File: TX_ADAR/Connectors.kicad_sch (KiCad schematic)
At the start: 10 parts, among them J1 Conn_Coaxial, J11 RJ45_LED_Shielded, J12 RJ45_LED_Shielded, J13 Conn_Coaxial, J14 Conn_Coaxial, J15 FX8-120S-SV21, J16 RJ45_LED_Shielded, J17 Conn_Coaxial, J18 Conn_Coaxial, J2 Conn_Coaxial

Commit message: Got footprints to work
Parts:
- J15: footprint FX8_120S_SV_21_:HRS_FX8-120S-SV_21_ -> footprints:CONN120_FX8-120S-SV_HIR
- J2: footprint (none) -> 142_1701_831:BEL_142-1701-831
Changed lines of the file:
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@@
 			)
 		)
-		(property "Footprint" "FX8_120S_SV_21_:HRS_FX8-120S-SV_21_"
+		(property "Footprint" "footprints:CONN120_FX8-120S-SV_HIR"
 			(at 146.05 20.32 0)
 			(hide yes)
@@
 			)
 		)
-		(property "Footprint" "FX8_120S_SV_21_:HRS_FX8-120S-SV_21_"
+		(property "Footprint" "footprints:CONN120_FX8-120S-SV_HIR"
 			(at 241.3 20.32 0)
 			(hide yes)
@@
 			)
 		)
-		(property "Footprint" ""
+		(property "Footprint" "142_1701_831:BEL_142-1701-831"
 			(at 57.15 19.05 0)
 			(hide yes)
@@
 			)
 		)
-		(property "Footprint" "FX8_120S_SV_21_:HRS_FX8-120S-SV_21_"
+		(property "Footprint" "footprints:CONN120_FX8-120S-SV_HIR"
 			(at 195.58 20.32 0)
 			(hide yes)

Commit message: Setting up layout plan
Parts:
- J15: footprint footprints:CONN120_FX8-120S-SV_HIR -> 120Conn footprints:CONN120_FX8-120S-SV_HIR
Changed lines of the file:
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@@
 			)
 		)
-		(property "Footprint" "footprints:CONN120_FX8-120S-SV_HIR"
+		(property "Footprint" "120Conn footprints:CONN120_FX8-120S-SV_HIR"
 			(at 146.05 20.32 0)
 			(hide yes)
@@
 			)
 		)
-		(property "Footprint" "footprints:CONN120_FX8-120S-SV_HIR"
+		(property "Footprint" "120Conn footprints:CONN120_FX8-120S-SV_HIR"
 			(at 241.3 20.32 0)
 			(hide yes)
@@
 			)
 		)
-		(property "Footprint" "footprints:CONN120_FX8-120S-SV_HIR"
+		(property "Footprint" "120Conn footprints:CONN120_FX8-120S-SV_HIR"
 			(at 195.58 20.32 0)
 			(hide yes)

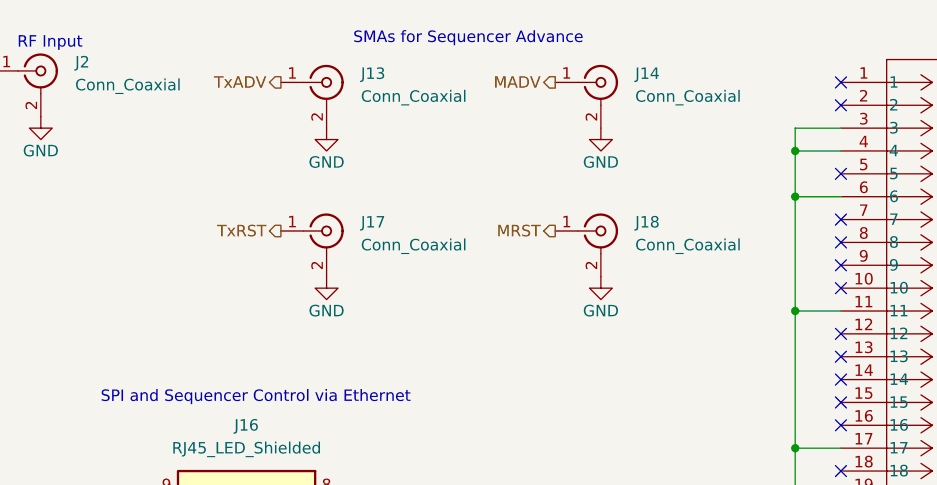
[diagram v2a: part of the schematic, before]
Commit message: Finished up adding footprints. Removed unnecessary switches for the TxRST and MRST
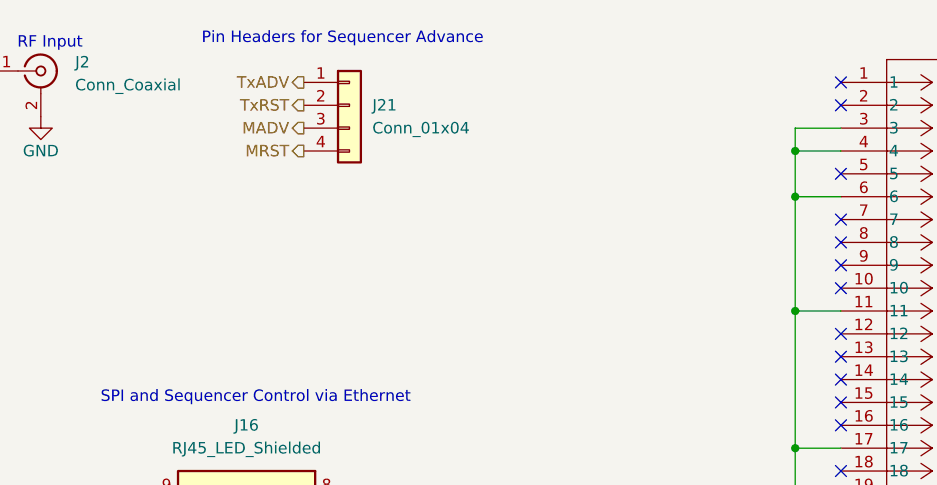
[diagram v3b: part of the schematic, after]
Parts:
- removed J13, J14, J17, J18: Conn_Coaxial, Connector_Coaxial:SMA_Amphenol_132134-10_Vertical, symbol Connector:Conn_Coaxial
- added J21: Conn_01x04, Connector_PinHeader_2.54mm:PinHeader_1x04_P2.54mm_Vertical, symbol Connector_Generic:Conn_01x04
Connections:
- net MADV: now also J21.3 (Pin_3)
- net MRST: now also J21.4 (Pin_4)
- net TxADV: now also J21.1 (Pin_1)
- net TxRST: now also J21.2 (Pin_2)
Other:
- note added: "Pin Headers for Sequencer Advance"
- note removed: "SMAs for Sequencer Advance"

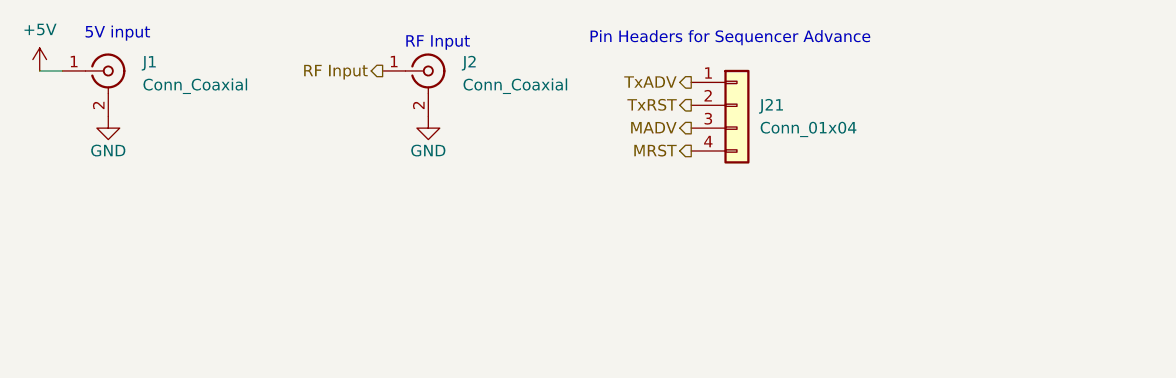
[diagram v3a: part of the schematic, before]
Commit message: Fixed footprint and meddled with the layout
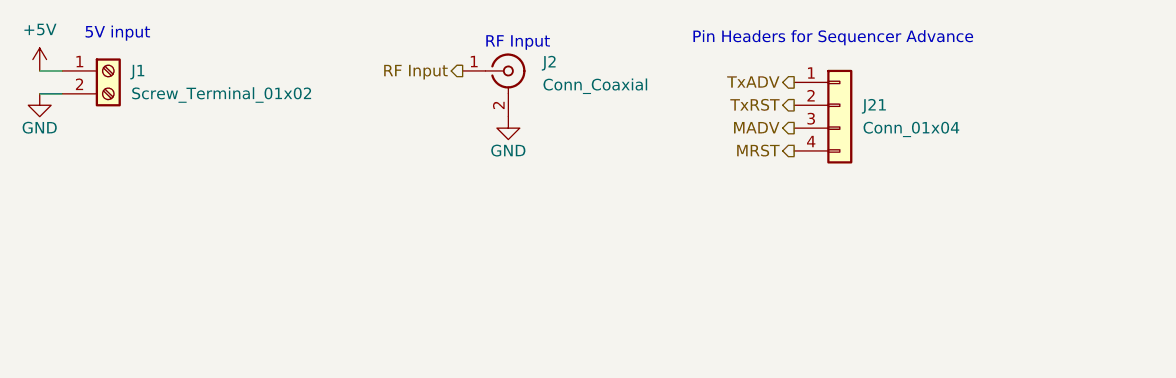
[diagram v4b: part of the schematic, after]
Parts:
- removed J1: Conn_Coaxial, Connector_Coaxial:SMA_Amphenol_132289_EdgeMount, symbol Connector:Conn_Coaxial
- added J1: Screw_Terminal_01x02, TerminalBlock_Phoenix:TerminalBlock_Phoenix_MKDS-1,5-2-5.08_1x02_P5.08mm_Horizontal, symbol Connector:Screw_Terminal_01x02
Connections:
- net +5V: now also J1.1 (Pin_1)
- net GND: now also J1.2 (Pin_2)
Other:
- moved on the sheet: J2, J21
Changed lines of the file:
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@@
 	(text "RF Input"
 		(exclude_from_sim no)
-		(at 58.166 16.002 0)
+		(at 67.056 16.002 0)
 		(effects
 			(font
@@
 	(text "Pin Headers for Sequencer Advance"
 		(exclude_from_sim no)
-		(at 90.678 15.494 0)
+		(at 102.108 15.494 0)
 		(effects
 			(font
@@
 	(wire
 		(pts
+			(xy 13.97 21.59) (xy 16.51 21.59)
+		)
+		(stroke
+			(width 0)
+			(type default)
+		)
+	)
+	(wire
+		(pts
 			(xy 236.22 116.84) (xy 241.3 116.84)
 		)
@@
 	(hierarchical_label "TxRST"
 		(shape output)
-		(at 86.36 22.86 180)
+		(at 97.79 22.86 180)
 		(effects
 			(font
@@
 	(hierarchical_label "MADV"
 		(shape output)
-		(at 86.36 25.4 180)
+		(at 97.79 25.4 180)
 		(effects
 			(font
@@
 	(hierarchical_label "RF Input"
 		(shape output)
-		(at 52.07 19.05 180)
+		(at 60.96 19.05 180)
 		(effects
 			(font
@@
 	(hierarchical_label "MRST"
 		(shape output)
-		(at 86.36 27.94 180)
+		(at 97.79 27.94 180)
 		(effects
 			(font
@@
 	(hierarchical_label "TxADV"
 		(shape output)
-		(at 86.36 20.32 180)
+		(at 97.79 20.32 180)
 		(effects
 			(font
@@
 	)
 	(symbol
+		(lib_id "Connector:Screw_Terminal_01x02")
+		(at 21.59 19.05 0)
+		(unit 1)
+		(body_style 1)
+		(exclude_from_sim no)
+		(in_bom yes)
+		(on_board yes)
+		(in_pos_files yes)
+		(dnp no)
+		(fields_autoplaced yes)
+		(property "Reference" "J1"
+			(at 24.13 19.0499 0)
+			(show_name no)
+			(do_not_autoplace no)
+			(effects
+				(font
+					(size 1.27 1.27)
+				)
+				(justify left)
+			)
+		)
+		(property "Value" "Screw_Terminal_01x02"
+			(at 24.13 21.5899 0)
+			(show_name no)
+			(do_not_autoplace no)
+			(effects
+				(font
+					(size 1.27 1.27)
+				)
+				(justify left)
+			)
+		)
+		(property "Footprint" "TerminalBlock_Phoenix:TerminalBlock_Phoenix_MKDS-1,5-2-5.08_1x02_P5.08mm_Horizontal"
+			(at 21.59 19.05 0)
+			(hide yes)
+			(show_name no)
+			(do_not_autoplace no)
+			(effects
+				(font
+					(size 1.27 1.27)
+				)
+			)
+		)
+		(property "Datasheet" ""
+			(at 21.59 19.05 0)
+			(hide yes)
+			(show_name no)
+			(do_not_autoplace no)
+			(effects
+				(font
+					(size 1.27 1.27)
+				)
+			)
+		)
+		(property "Description" "Generic screw terminal, single row, 01x02, script generated (kicad-library-utils/schlib/autogen/connector/)"
+			(at 21.59 19.05 0)
+			(hide yes)
+			(show_name no)
+			(do_not_autoplace no)
+			(effects
+				(font
+					(size 1.27 1.27)
+				)
+			)
+		)
+		(pin "1"
+		)
+		(pin "2"
+		)
+		(instances
+			(project "TX_ADAR"
+				(path "/5bb7bcfe-c6dc-48dd-b109-2cc47fd52212/5711866b-ad81-4828-9e56-17f3c1154618"
+					(reference "J1")
+					(unit 1)
+				)
+			)
+		)
+	)
+	(symbol
 		(lib_id "power:PWR_FLAG")
 		(at 40.64 66.04 0)
@@
 	(symbol
 		(lib_id "Connector_Generic:Conn_01x04")
-		(at 91.44 22.86 0)
+		(at 102.87 22.86 0)
 		(unit 1)
 		(body_style 1)
@@
 		(fields_autoplaced yes)
 		(property "Reference" "J21"
-			(at 93.98 22.86 0)
+			(at 105.41 22.86 0)
 			(show_name no)
 			(do_not_autoplace no)
@@
 		)
 		(property "Value" "Conn_01x04"
-			(at 93.98 25.4 0)
+			(at 105.41 25.4 0)
 			(show_name no)
 			(do_not_autoplace no)
@@
 		)
 		(property "Footprint" "Connector_PinHeader_2.54mm:PinHeader_1x04_P2.54mm_Vertical"
-			(at 91.44 22.86 0)
+			(at 102.87 22.86 0)
 			(hide yes)
 			(show_name no)
@@
 		)
 		(property "Datasheet" ""
-			(at 91.44 22.86 0)
+			(at 102.87 22.86 0)
 			(hide yes)
 			(show_name no)
@@
 		)
 		(property "Description" "Generic connector, single row, 01x04, script generated (kicad-library-utils/schlib/autogen/connector/)"
-			(at 91.44 22.86 0)
+			(at 102.87 22.86 0)
 			(hide yes)
 			(show_name no)
@@
 	(symbol
 		(lib_id "Connector:Conn_Coaxial")
-		(at 57.15 19.05 0)
+		(at 66.04 19.05 0)
 		(unit 1)
 		(body_style 1)
@@
 		(fields_autoplaced yes)
 		(property "Reference" "J2"
-			(at 60.96 18.0731 0)
+			(at 69.85 18.0731 0)
 			(show_name no)
 			(do_not_autoplace no)
@@
 		)
 		(property "Value" "Conn_Coaxial"
-			(at 60.96 20.6131 0)
+			(at 69.85 20.6131 0)
 			(show_name no)
 			(do_not_autoplace no)
@@
 		)
 		(property "Footprint" "142_1701_831:BEL_142-1701-831"
-			(at 57.15 19.05 0)
+			(at 66.04 19.05 0)
 			(hide yes)
 			(show_name no)
@@
 		)
 		(property "Datasheet" ""
-			(at 57.15 19.05 0)
+			(at 66.04 19.05 0)
 			(hide yes)
 			(show_name no)
@@
 		)
 		(property "Description" "coaxial connector (BNC, SMA, SMB, SMC, Cinch/RCA, LEMO, ...)"
-			(at 57.15 19.05 0)
+			(at 66.04 19.05 0)
 			(hide yes)
 			(show_name no)
@@
 	)
 	(symbol
-		(lib_id "Connector:Conn_Coaxial")
-		(at 21.59 19.05 0)
-		(unit 1)
-		(body_style 1)
-		(exclude_from_sim no)
-		(in_bom yes)
-		(on_board yes)
-		(in_pos_files yes)
-		(dnp no)
-		(fields_autoplaced yes)
-		(property "Reference" "J1"
-			(at 25.4 18.0731 0)
-			(show_name no)
-			(do_not_autoplace no)
-			(effects
-				(font
-					(size 1.27 1.27)
-				)
-				(justify left)
-			)
-		)
-		(property "Value" "Conn_Coaxial"
-			(at 25.4 20.6131 0)
-			(show_name no)
-			(do_not_autoplace no)
-			(effects
-				(font
-					(size 1.27 1.27)
-				)
-				(justify left)
-			)
-		)
-		(property "Footprint" "Connector_Coaxial:SMA_Amphenol_132289_EdgeMount"
-			(at 21.59 19.05 0)
-			(hide yes)
-			(show_name no)
-			(do_not_autoplace no)
-			(effects
-				(font
-					(size 1.27 1.27)
-				)
-			)
-		)
-		(property "Datasheet" ""
-			(at 21.59 19.05 0)
-			(hide yes)
-			(show_name no)
-			(do_not_autoplace no)
-			(effects
-				(font
-					(size 1.27 1.27)
-				)
-			)
-		)
-		(property "Description" "coaxial connector (BNC, SMA, SMB, SMC, Cinch/RCA, LEMO, ...)"
-			(at 21.59 19.05 0)
-			(hide yes)
-			(show_name no)
-			(do_not_autoplace no)
-			(effects
-				(font
-					(size 1.27 1.27)
-				)
-			)
-		)
-		(pin "1"
-		)
-		(pin "2"
-		)
-		(instances
-			(project "TX_ADAR"
-				(path "/5bb7bcfe-c6dc-48dd-b109-2cc47fd52212/5711866b-ad81-4828-9e56-17f3c1154618"
-					(reference "J1")
-					(unit 1)
-				)
-			)
-		)
-	)
-	(symbol
 		(lib_id "power:GND")
-		(at 57.15 24.13 0)
+		(at 66.04 24.13 0)
 		(unit 1)
 		(body_style 1)
@@
 		(dnp no)
 		(property "Reference" "#PWR010"
-			(at 57.15 30.48 0)
+			(at 66.04 30.48 0)
 			(hide yes)
 			(show_name no)
@@
 		)
 		(property "Value" "GND"
-			(at 57.15 27.94 0)
+			(at 66.04 27.94 0)
 			(show_name no)
 			(do_not_autoplace no)
@@
 		)
 		(property "Footprint" ""
-			(at 57.15 24.13 0)
+			(at 66.04 24.13 0)
 			(hide yes)
 			(show_name no)
@@
 		)
 		(property "Datasheet" ""
-			(at 57.15 24.13 0)
+			(at 66.04 24.13 0)
 			(hide yes)
 			(show_name no)
@@
 		)
 		(property "Description" "Power symbol creates a global label with name \"GND\" , ground"
-			(at 57.15 24.13 0)
+			(at 66.04 24.13 0)
 			(hide yes)
 			(show_name no)
@@
 	(symbol
 		(lib_id "power:GND")
-		(at 21.59 24.13 0)
+		(at 13.97 21.59 0)
 		(unit 1)
 		(body_style 1)
@@
 		(dnp no)
 		(property "Reference" "#PWR09"
-			(at 21.59 30.48 0)
+			(at 13.97 27.94 0)
 			(hide yes)
 			(show_name no)
@@
 		)
 		(property "Value" "GND"
-			(at 21.59 27.94 0)
+			(at 13.97 25.4 0)
 			(show_name no)
 			(do_not_autoplace no)
@@
 		)
 		(property "Footprint" ""
-			(at 21.59 24.13 0)
+			(at 13.97 21.59 0)
 			(hide yes)
 			(show_name no)
@@
 		)
 		(property "Datasheet" ""
-			(at 21.59 24.13 0)
+			(at 13.97 21.59 0)
 			(hide yes)
 			(show_name no)
@@
 		)
 		(property "Description" "Power symbol creates a global label with name \"GND\" , ground"
-			(at 21.59 24.13 0)
+			(at 13.97 21.59 0)
 			(hide yes)
 			(show_name no)

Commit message: Layout updates
Using vias to connect hard to reach spots
Added copper pours
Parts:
- J2: footprint 142_1701_831:BEL_142-1701-831 -> CON292001_1:TE_CON292001-1
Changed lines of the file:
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@@
 			)
 		)
-		(property "Footprint" "142_1701_831:BEL_142-1701-831"
+		(property "Footprint" "CON292001_1:TE_CON292001-1"
 			(at 66.04 19.05 0)
 			(hide yes)
